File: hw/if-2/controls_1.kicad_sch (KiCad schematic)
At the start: 17 parts, among them Q11 MMBT3904, Q12 MMBT3904, U12 LTV-356T

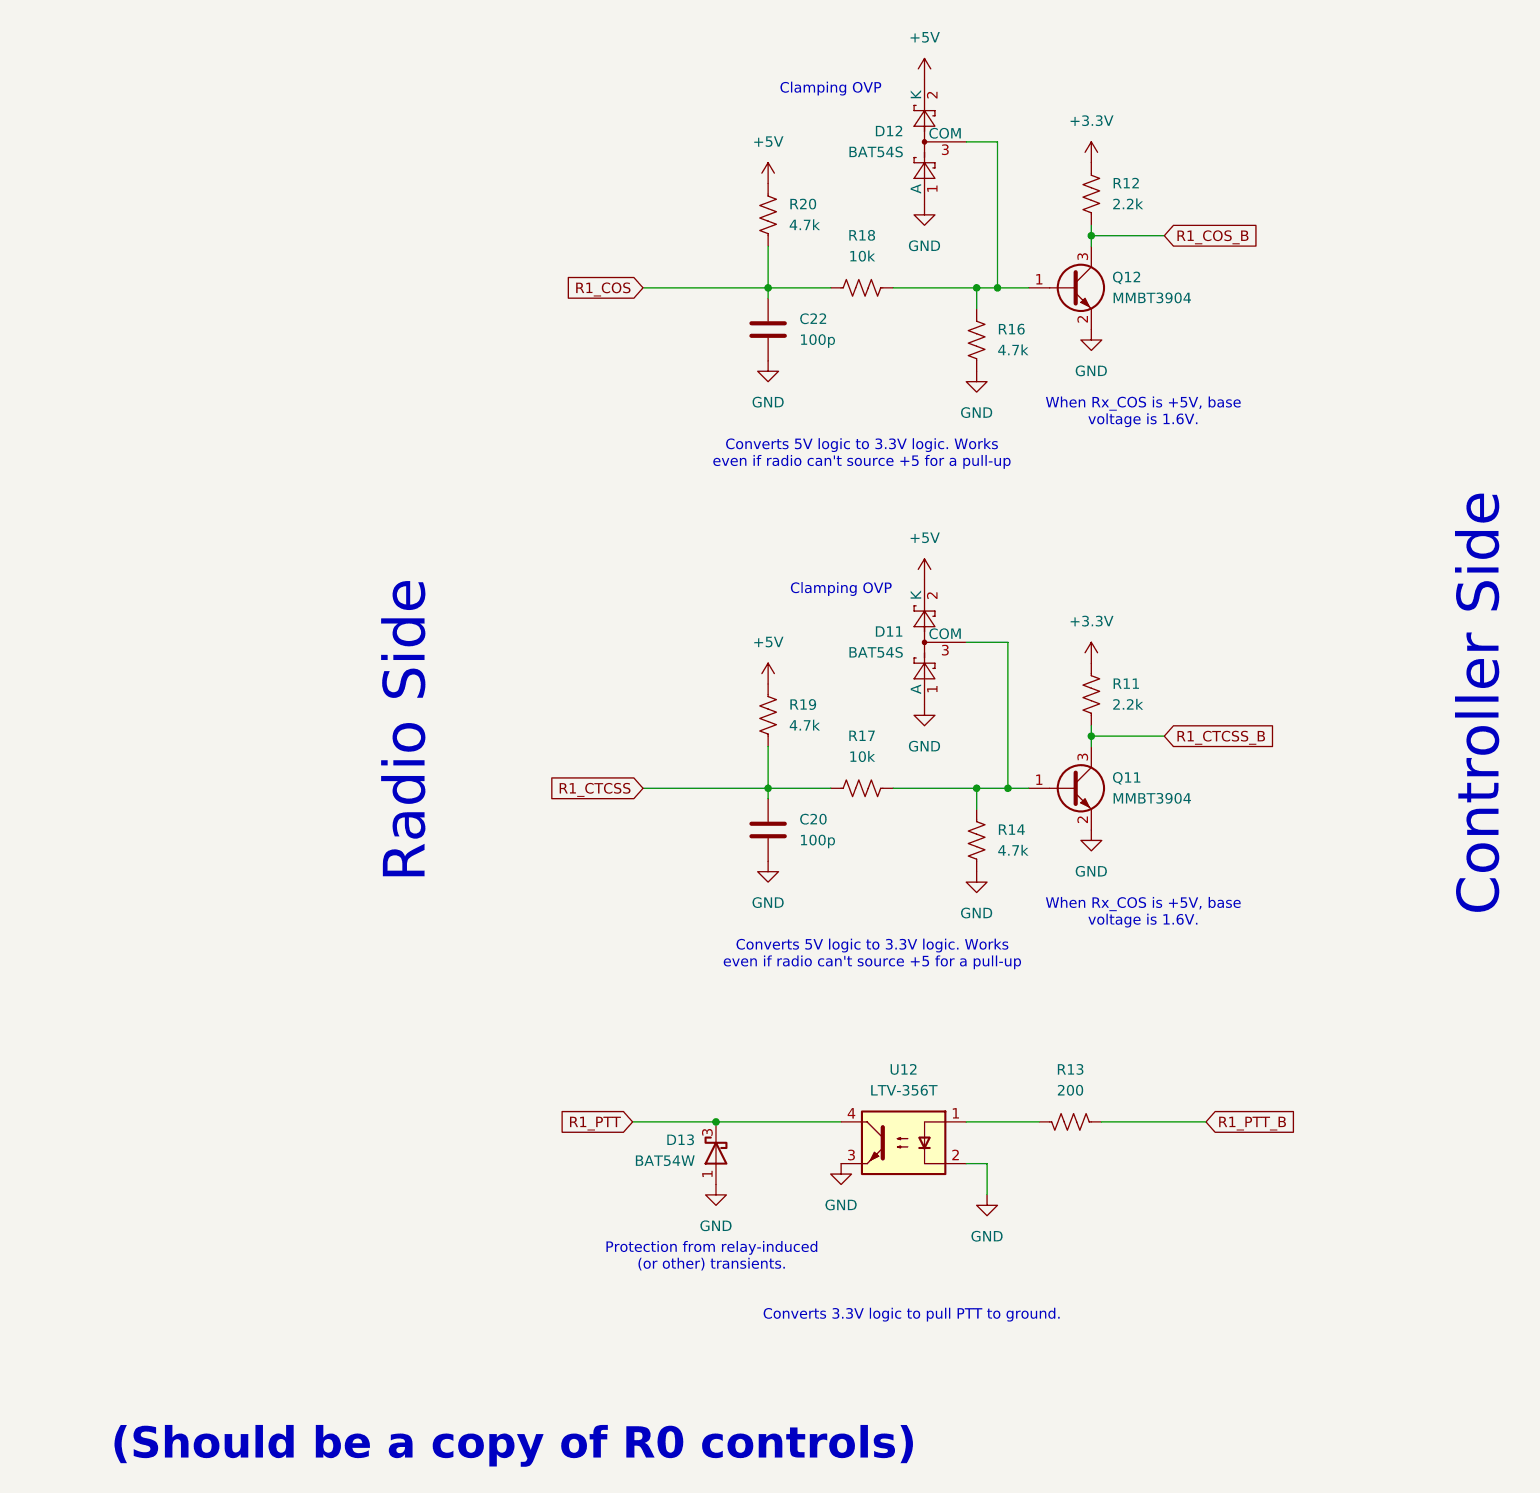
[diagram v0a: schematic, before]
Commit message: Documentation improvements, moved a OVP circuit
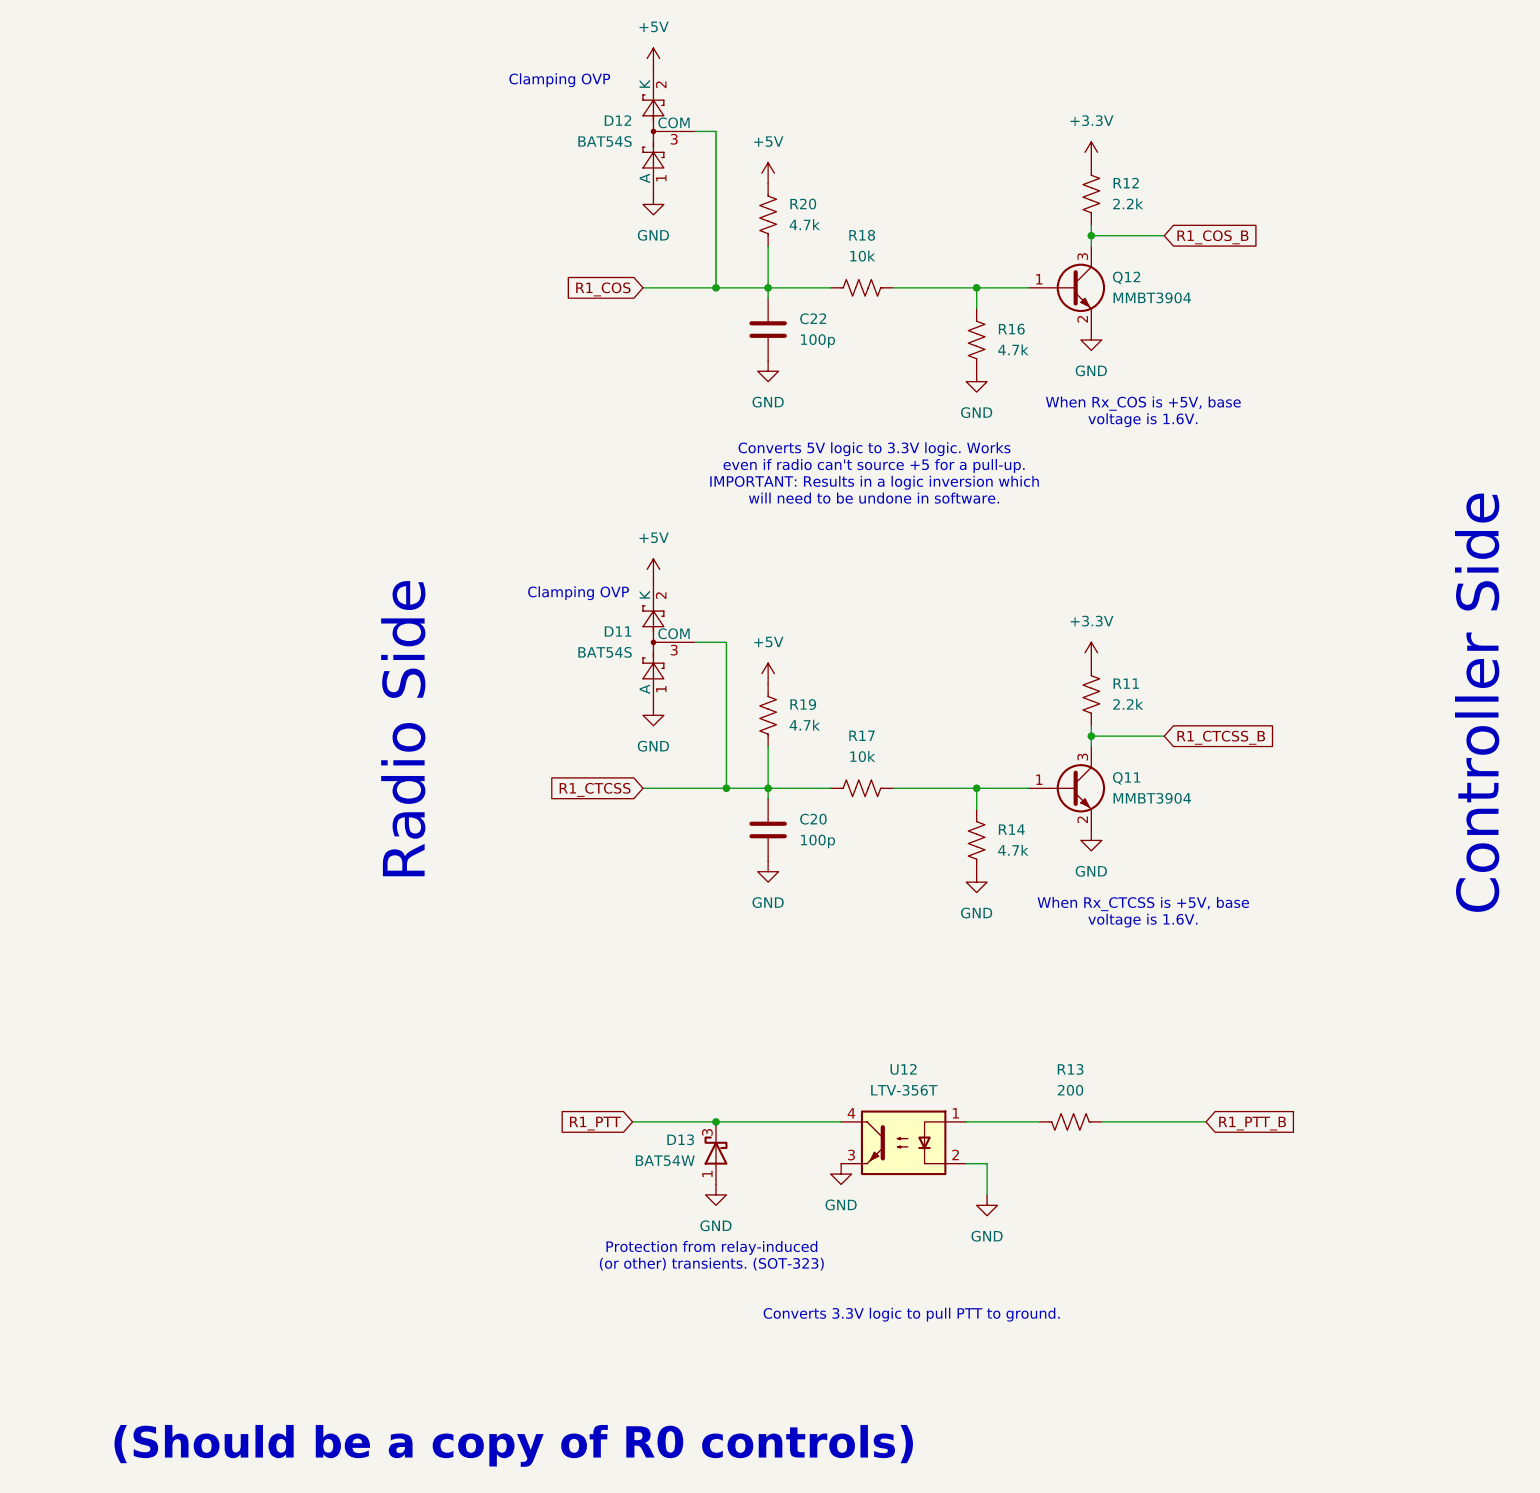
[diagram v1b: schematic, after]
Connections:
- net R1_COS: now also D12.3 (COM)
- net R1_CTCSS: now also D11.3 (COM)
- net at Q12.1 (B), R16.1, R18.2: no longer D12.3 (COM)
- net at Q11.1 (B), R14.1, R17.2: no longer D11.3 (COM)
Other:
- note added: "Converts 5V logic to 3.3V logic. Works even if radio can't source +5 for a pull-up. IMPORTANT: Results in a logic inversion which will need to be undone in software."
- note added: "Protection from relay-induced (or other) transients. (SOT-323)"
- note added: "When Rx_CTCSS is +5V, base voltage is 1.6V."
- note removed: "Converts 5V logic to 3.3V logic. Works even if radio can't source +5 for a pull-up"
- note removed: "Protection from relay-induced (or other) transients."
- moved on the sheet: D11, D12

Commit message: Updating schematics, create new mini-board for radio interface
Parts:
- removed U12: LTV-356T, Package_SO:SO-4_4.4x3.6mm_P2.54mm, symbol Isolator:LTV-356T
- added Q14: 2N7002, Package_TO_SOT_SMD:SOT-23, symbol Transistor_FET:2N7002
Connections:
- net GND: now also Q14.2 (S)
- net R1_PTT: now also Q14.3 (D)
- net at R13.2: now also Q14.1 (G)
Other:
- note added: "I_{DS} max is 220mA, V_{DS} max is 60V."
- moved on the sheet: D13
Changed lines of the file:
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@@
 	(text "Protection from relay-induced \n(or other) transients. (SOT-323)"
 		(exclude_from_sim no)
-		(at 102.362 167.64 0)
+		(at 96.012 162.56 0)
 		(effects
 			(font
@@
 	(text "Converts 3.3V logic to pull PTT to ground."
 		(exclude_from_sim no)
-		(at 126.746 174.752 0)
+		(at 128.524 168.91 0)
 		(effects
 			(font
@@
 		)
 	)
+	(text "I_{DS} max is 220mA, V_{DS} max is 60V."
+		(exclude_from_sim no)
+		(at 124.968 141.732 0)
+		(effects
+			(font
+				(size 1.27 1.27)
+				(color 255 5 9 1)
+			)
+		)
+	)
 	(junction
-		(at 102.87 151.13)
+		(at 96.52 146.05)
 		(diameter 0)
 		(color 0 0 0 0)
@@
 	(wire
 		(pts
-			(xy 133.35 156.21) (xy 135.89 156.21)
-		)
-		(stroke
-			(width 0)
-			(type default)
-		)
-	)
-	(wire
-		(pts
 			(xy 134.62 49.53) (xy 134.62 52.07)
 		)
@@
 	(wire
 		(pts
-			(xy 118.11 151.13) (xy 102.87 151.13)
+			(xy 96.52 146.05) (xy 125.73 146.05)
 		)
 		(stroke
@@
 	(wire
 		(pts
-			(xy 102.87 151.13) (xy 92.71 151.13)
+			(xy 96.52 146.05) (xy 86.36 146.05)
 		)
 		(stroke
@@
 		(pts
 			(xy 109.22 105.41) (xy 109.22 110.49)
-		)
-		(stroke
-			(width 0)
-			(type default)
-		)
-	)
-	(wire
-		(pts
-			(xy 135.89 156.21) (xy 135.89 160.02)
 		)
 		(stroke
@@
 	(global_label "R1_PTT"
 		(shape input)
-		(at 92.71 151.13 180)
+		(at 86.36 146.05 180)
 		(fields_autoplaced yes)
 		(effects
@@
 		)
 		(property "Intersheetrefs" "${INTERSHEET_REFS}"
-			(at 83.0725 151.13 0)
+			(at 76.7225 146.05 0)
 			(effects
 				(font
@@
 	(symbol
 		(lib_id "Diode:BAT54W")
-		(at 102.87 154.94 90)
+		(at 96.52 149.86 90)
 		(mirror x)
 		(unit 1)
@@
 		(fields_autoplaced yes)
 		(property "Reference" "D13"
-			(at 100.33 153.3524 90)
+			(at 93.98 148.2724 90)
 			(effects
 				(font
@@
 		)
 		(property "Value" "BAT54W"
-			(at 100.33 155.8924 90)
+			(at 93.98 150.8124 90)
 			(effects
 				(font
@@
 		)
 		(property "Footprint" "Package_TO_SOT_SMD:SOT-323_SC-70"
-			(at 107.315 154.94 0)
+			(at 100.965 149.86 0)
 			(effects
 				(font
@@
 		)
 		(property "Datasheet" "https://assets.nexperia.com/documents/data-sheet/BAT54W_SER.pdf"
-			(at 102.87 154.94 0)
+			(at 96.52 149.86 0)
 			(effects
 				(font
@@
 		)
 		(property "Description" "Schottky barrier diode, SOT-323"
-			(at 102.87 154.94 0)
+			(at 96.52 149.86 0)
 			(effects
 				(font
@@
 	)
 	(symbol
-		(lib_id "Isolator:LTV-356T")
-		(at 125.73 153.67 0)
-		(mirror y)
-		(unit 1)
-		(exclude_from_sim no)
-		(in_bom yes)
-		(on_board yes)
-		(dnp no)
-		(fields_autoplaced yes)
-		(property "Reference" "U12"
-			(at 125.73 144.78 0)
-			(effects
-				(font
-					(size 1.27 1.27)
-				)
-			)
-		)
-		(property "Value" "LTV-356T"
-			(at 125.73 147.32 0)
-			(effects
-				(font
-					(size 1.27 1.27)
-				)
-			)
-		)
-		(property "Footprint" "Package_SO:SO-4_4.4x3.6mm_P2.54mm"
-			(at 130.81 158.75 0)
-			(effects
-				(font
-					(size 1.27 1.27)
-					(italic yes)
-				)
-				(justify left)
-				(hide yes)
-			)
-		)
-		(property "Datasheet" "http://optoelectronics.liteon.com/upload/download/DS70-2001-010/S_110_LTV-356T%2020140520.pdf"
-			(at 125.73 153.67 0)
-			(effects
-				(font
-					(size 1.27 1.27)
-				)
-				(justify left)
-				(hide yes)
-			)
-		)
-		(property "Description" "DC Optocoupler, Vce 80V, CTR 50%, SO-4"
-			(at 125.73 153.67 0)
-			(effects
-				(font
-					(size 1.27 1.27)
-				)
-				(hide yes)
-			)
-		)
-		(pin "1"
-		)
-		(pin "2"
-		)
-		(pin "3"
-		)
-		(pin "4"
-		)
-		(instances
-			(project "if-2"
-				(path "/a8c2d6aa-29bb-49bd-a367-0d62a0a32480/aaca03b7-1394-4a9e-b9db-1ef93c5c7c02"
-					(reference "U12")
-					(unit 1)
-				)
-			)
-		)
-	)
-	(symbol
 		(lib_id "Device:R_US")
 		(at 134.62 55.88 0)
@@
 	(symbol
 		(lib_id "power:GND")
-		(at 118.11 156.21 0)
+		(at 125.73 156.21 0)
 		(mirror y)
 		(unit 1)
@@
 		(fields_autoplaced yes)
 		(property "Reference" "#PWR067"
-			(at 118.11 162.56 0)
+			(at 125.73 162.56 0)
 			(effects
 				(font
@@
 		)
 		(property "Value" "GND"
-			(at 118.11 161.29 0)
+			(at 125.73 161.29 0)
 			(effects
 				(font
@@
 		)
 		(property "Footprint" ""
-			(at 118.11 156.21 0)
+			(at 125.73 156.21 0)
 			(effects
 				(font
@@
 		)
 		(property "Datasheet" ""
-			(at 118.11 156.21 0)
+			(at 125.73 156.21 0)
 			(effects
 				(font
@@
 		)
 		(property "Description" "Power symbol creates a global label with name \"GND\" , ground"
-			(at 118.11 156.21 0)
+			(at 125.73 156.21 0)
 			(effects
 				(font
@@
 	)
 	(symbol
+		(lib_id "Transistor_FET:2N7002")
+		(at 128.27 151.13 0)
+		(mirror y)
+		(unit 1)
+		(exclude_from_sim no)
+		(in_bom yes)
+		(on_board yes)
+		(dnp no)
+		(property "Reference" "Q14"
+			(at 132.588 147.066 0)
+			(effects
+				(font
+					(size 1.27 1.27)
+				)
+				(justify left)
+			)
+		)
+		(property "Value" "2N7002"
+			(at 134.62 145.034 0)
+			(effects
+				(font
+					(size 1.27 1.27)
+				)
+				(justify left)
+			)
+		)
+		(property "Footprint" "Package_TO_SOT_SMD:SOT-23"
+			(at 123.19 153.035 0)
+			(effects
+				(font
+					(size 1.27 1.27)
+					(italic yes)
+				)
+				(justify left)
+				(hide yes)
+			)
+		)
+		(property "Datasheet" "https://www.onsemi.com/pub/Collateral/NDS7002A-D.PDF"
+			(at 123.19 154.94 0)
+			(effects
+				(font
+					(size 1.27 1.27)
+				)
+				(justify left)
+				(hide yes)
+			)
+		)
+		(property "Description" "0.115A Id, 60V Vds, N-Channel MOSFET, SOT-23"
+			(at 128.27 151.13 0)
+			(effects
+				(font
+					(size 1.27 1.27)
+				)
+				(hide yes)
+			)
+		)
+		(pin "2"
+		)
+		(pin "3"
+		)
+		(pin "1"
+		)
+		(instances
+			(project "if-2"
+				(path "/a8c2d6aa-29bb-49bd-a367-0d62a0a32480/aaca03b7-1394-4a9e-b9db-1ef93c5c7c02"
+					(reference "Q14")
+					(unit 1)
+				)
+			)
+		)
+	)
+	(symbol
 		(lib_id "power:GND")
 		(at 109.22 119.38 0)
@@
 	(symbol
 		(lib_id "power:GND")
-		(at 102.87 158.75 0)
+		(at 96.52 153.67 0)
 		(mirror y)
 		(unit 1)
@@
 		(fields_autoplaced yes)
 		(property "Reference" "#PWR0154"
-			(at 102.87 165.1 0)
+			(at 96.52 160.02 0)
 			(effects
 				(font
@@
 		)
 		(property "Value" "GND"
-			(at 102.87 163.83 0)
+			(at 96.52 158.75 0)
 			(effects
 				(font
@@
 		)
 		(property "Footprint" ""
-			(at 102.87 158.75 0)
+			(at 96.52 153.67 0)
 			(effects
 				(font
@@
 		)
 		(property "Datasheet" ""
-			(at 102.87 158.75 0)
+			(at 96.52 153.67 0)
 			(effects
 				(font
@@
 		)
 		(property "Description" "Power symbol creates a global label with name \"GND\" , ground"
-			(at 102.87 158.75 0)
+			(at 96.52 153.67 0)
 			(effects
 				(font
@@
 					(unit 1)
 				)
-			)
-		)
-	)
-	(symbol
-		(lib_id "power:GND")
-		(at 135.89 160.02 0)
-		(mirror y)
-		(unit 1)
-		(exclude_from_sim no)
-		(in_bom yes)
-		(on_board yes)
-		(dnp no)
-		(fields_autoplaced yes)
-		(property "Reference" "#PWR016"
-			(at 135.89 166.37 0)
-			(effects
-				(font
-					(size 1.27 1.27)
-				)
-				(hide yes)
-			)
-		)
-		(property "Value" "GND"
-			(at 135.89 165.1 0)
-			(effects
-				(font
-					(size 1.27 1.27)
-				)
-			)
-		)
-		(property "Footprint" ""
-			(at 135.89 160.02 0)
-			(effects
-				(font
-					(size 1.27 1.27)
-				)
-				(hide yes)
-			)
-		)
-		(property "Datasheet" ""
-			(at 135.89 160.02 0)
-			(effects
-				(font
-					(size 1.27 1.27)
-				)
-				(hide yes)
-			)
-		)
-		(property "Description" "Power symbol creates a global label with name \"GND\" , ground"
-			(at 135.89 160.02 0)
-			(effects
-				(font
-					(size 1.27 1.27)
-				)
-				(hide yes)
-			)
-		)
-		(pin "1"
-		)
-		(instances
-			(project "if-2"
-				(path "/a8c2d6aa-29bb-49bd-a367-0d62a0a32480/aaca03b7-1394-4a9e-b9db-1ef93c5c7c02"
-					(reference "#PWR016")
-					(unit 1)
-				)
